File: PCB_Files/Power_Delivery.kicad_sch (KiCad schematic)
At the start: 0 parts

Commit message: Began laying out power schematic and motor controller schematic
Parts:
- added 5V_Buck_Module: Screw_Terminal_01x04, symbol Connector:Screw_Terminal_01x04
- added BT1: Battery, symbol Device:Battery
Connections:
- new net +5V: 5V_Buck_Module.2 (Pin_2)
- new net +BATT: 5V_Buck_Module.1 (Pin_1), BT1.1 (+)
- new net GND: 5V_Buck_Module.3 (Pin_3), 5V_Buck_Module.4 (Pin_4), BT1.2 (-)
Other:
- note added: "8V4 (Full) - 7V4 (Nom) - 6V4 (Cutoff)"

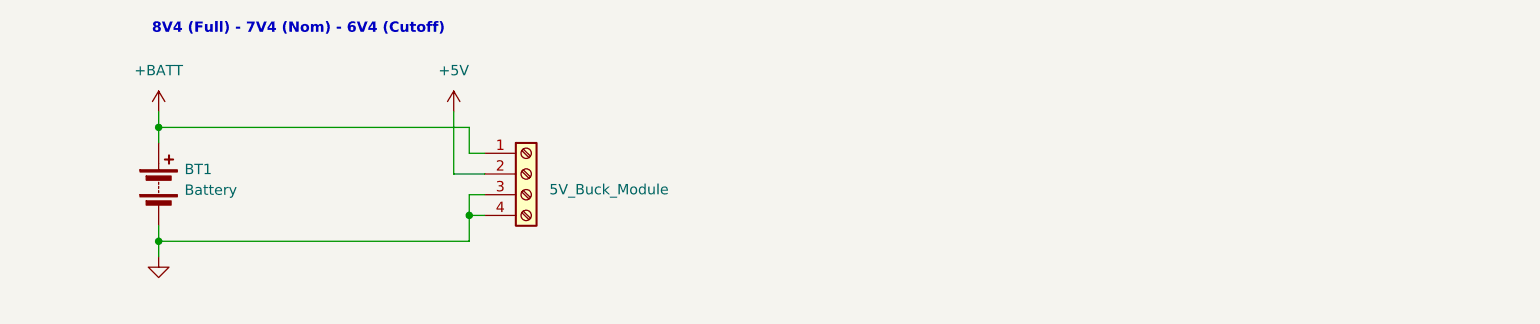
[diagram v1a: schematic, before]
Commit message: Completed power schematic page. 2S LiPo to buck module to LDO regulator for 3.3v
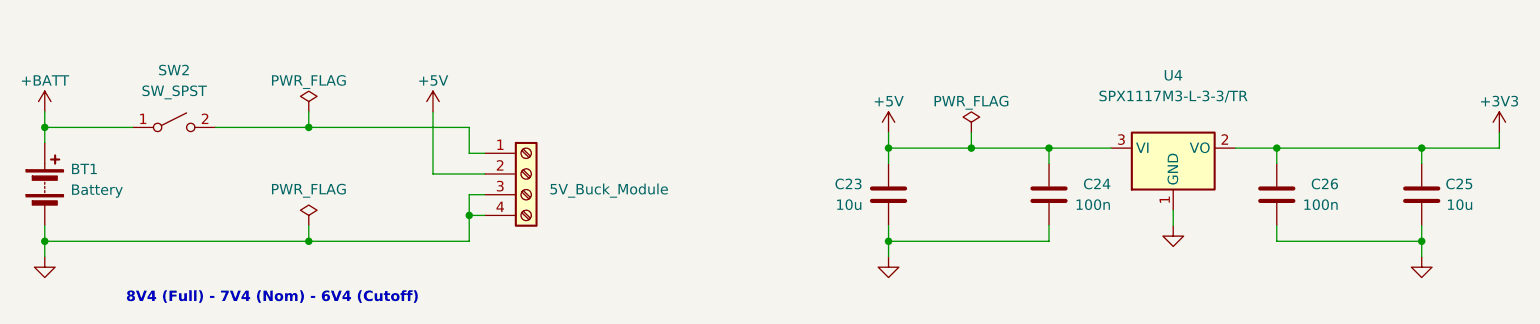
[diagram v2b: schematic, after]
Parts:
- added C23, C25: 10u, symbol Device:C
- added C24, C26: 100n, symbol Device:C
- added SW2: SW_SPST, symbol Switch:SW_SPST
- added U4: SPX1117M3-L-3-3/TR, Package_TO_SOT_SMD:SOT-223-3_TabPin2, symbol Regulator_Linear:AMS1117-3.3
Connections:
- net +5V: now also C23.1, C24.1, U4.3 (VI)
- net +BATT: now also SW2.1 (A); no longer 5V_Buck_Module.1 (Pin_1)
- net GND: now also C23.2, C24.2, C25.2, C26.2, U4.1 (GND)
- new net: 5V_Buck_Module.1 (Pin_1), SW2.2 (B)
- new net +3V3: C25.1, C26.1, U4.2 (VO)
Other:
- moved on the sheet: BT1

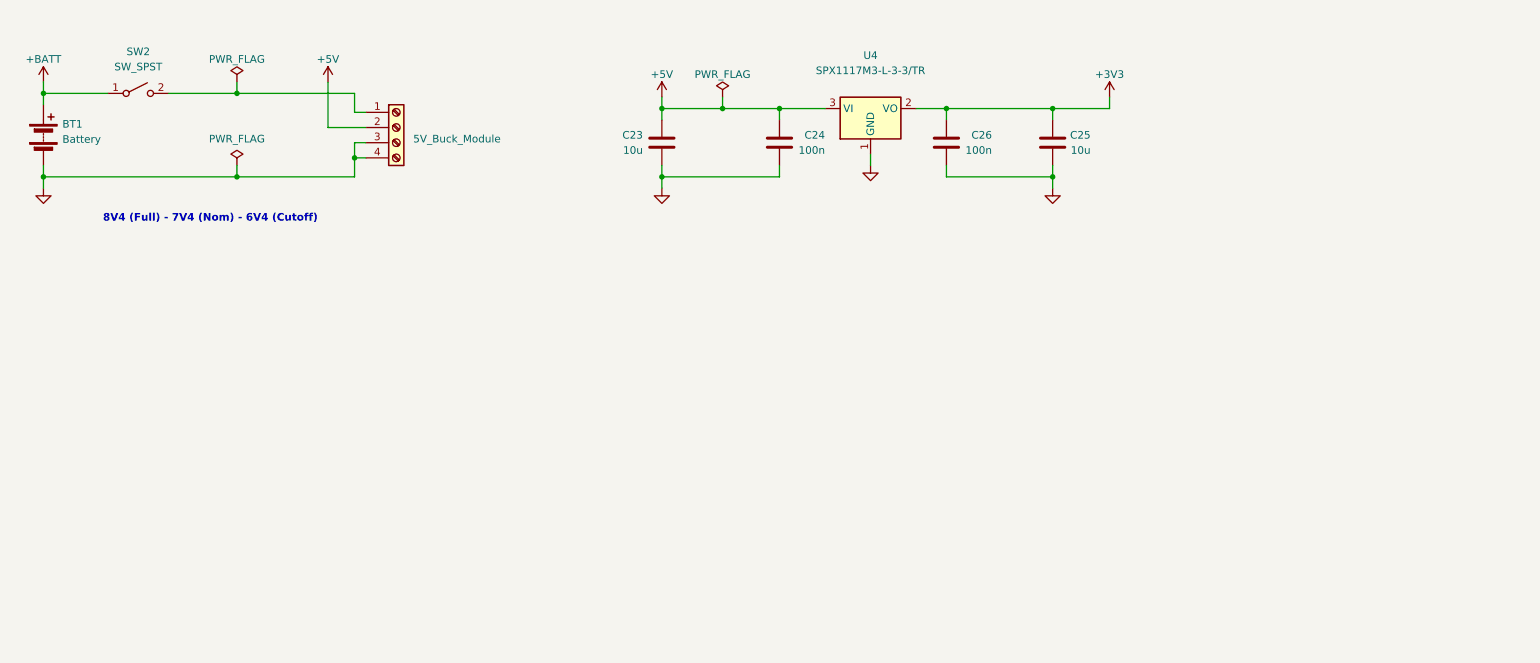
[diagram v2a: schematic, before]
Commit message: Cleaned up all ERC errors and warnings due to missing Power Flags or misaligned grid.
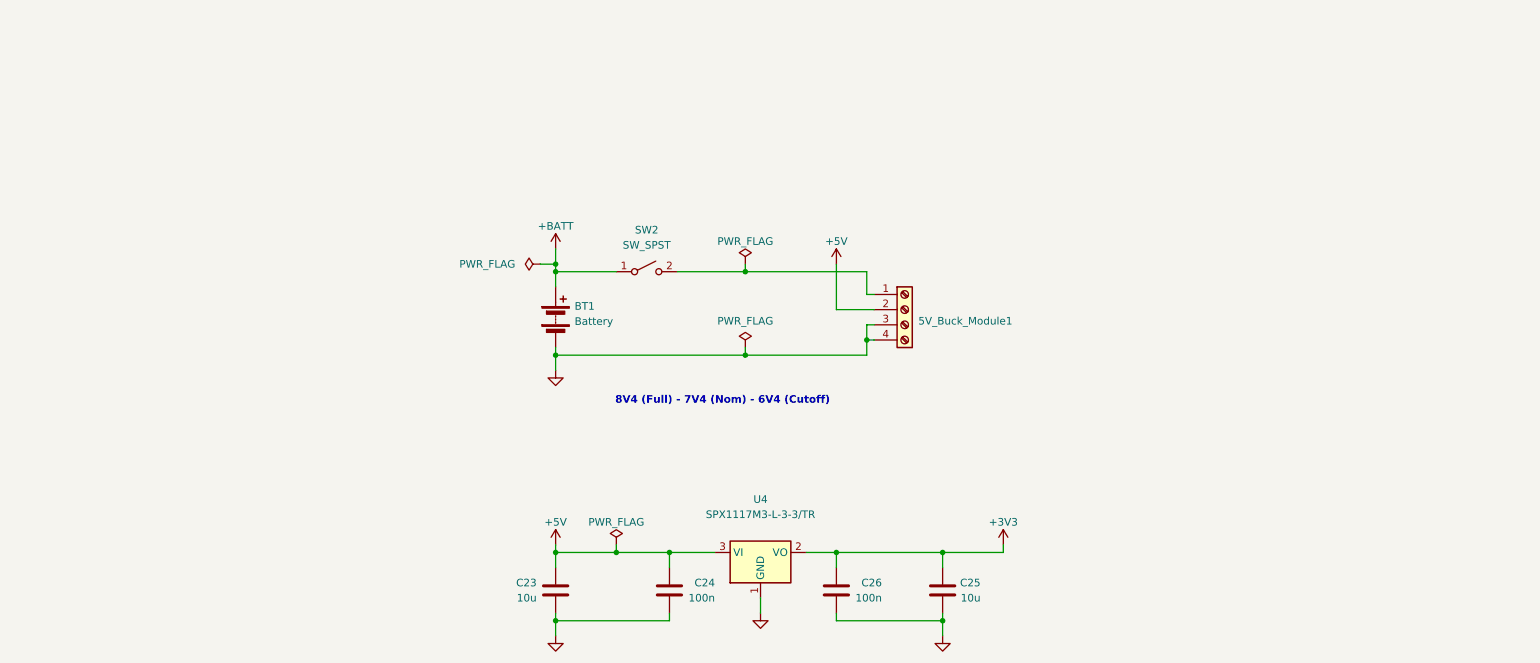
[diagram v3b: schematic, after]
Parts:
- renumbered 5V_Buck_Module to 5V_Buck_Module1
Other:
- moved on the sheet: 5V_Buck_Module1, BT1, C23, C24, C25, C26, SW2, U4

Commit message: General schematic clean up and footprint allocation.
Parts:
- C23, C24, C25, C26: footprint (none) -> Capacitor_SMD:C_0603_1608Metric
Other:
- moved on the sheet: 5V_Buck_Module1, BT1, C23, C24, C25, C26, SW2, U4

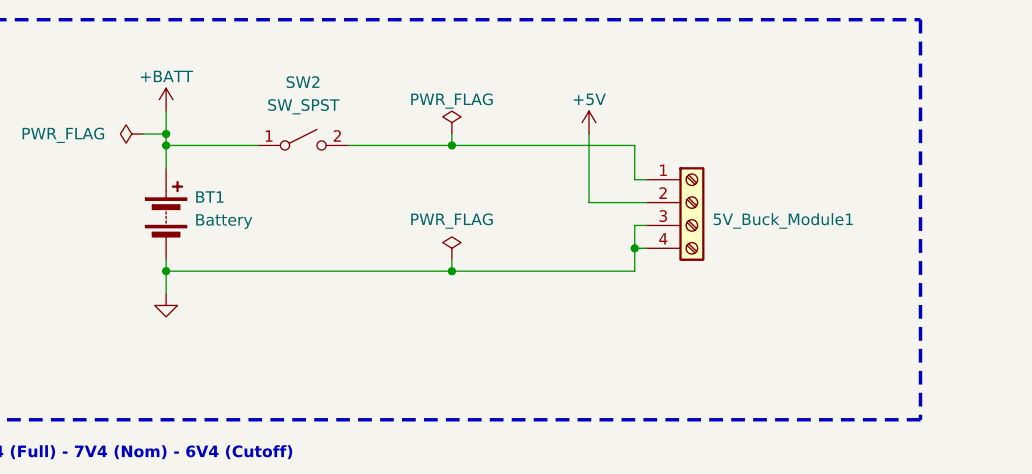
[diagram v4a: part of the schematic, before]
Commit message: Added RadioMaster 2S Battery information to power schematic sheet.
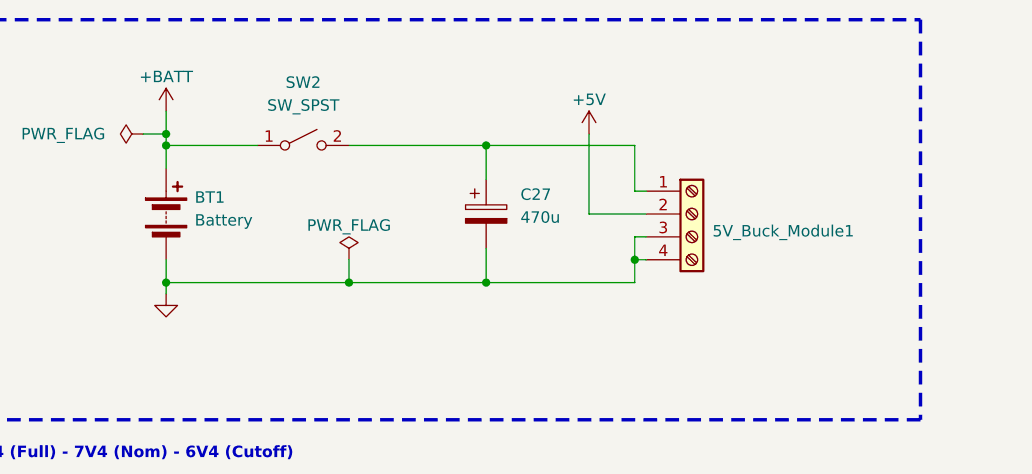
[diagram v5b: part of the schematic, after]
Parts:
- added C27: 470u, symbol Device:C_Polarized
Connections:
- net GND: now also C27.2
- net at 5V_Buck_Module1.1 (Pin_1), SW2.2 (B): now also C27.1
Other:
- moved on the sheet: 5V_Buck_Module1

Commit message: Cleaned up MCU sheet, added bounding boxes for peripherals.
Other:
- note added: "BATTERY INFO - Capacity: 5000mAh Watt Hours: 37wh Voltage: 7.4V Cells: 2 x 21700 Li-ion 3.7V 18.5Wh Connector: JST-XH and XT30 Charge current: Max 2A Dimensions: 71.5 x 43.5 x 23.5 mm Weight: 155g"
- note added: "RadioMaster 5000mAh 2s Li-ion"
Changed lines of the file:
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@@
 	(text "8V4 (Full) - 7V4 (Nom) - 6V4 (Cutoff)"
 		(exclude_from_sim no)
-		(at 38.1 80.01 0)
+		(at 38.1 85.09 0)
 		(effects
 			(font
@@
 		)
 	)
+	(text "RadioMaster 5000mAh 2s Li-ion"
+		(exclude_from_sim no)
+		(at 34.29 81.28 0)
+		(effects
+			(font
+				(size 1.27 1.27)
+				(thickness 0.254)
+				(bold yes)
+			)
+		)
+	)
+	(text "BATTERY INFO -\n\nCapacity: 5000mAh\n\nWatt Hours: 37wh\n\nVoltage: 7.4V\n\nCells: 2 x 21700 Li-ion 3.7V 18.5Wh\n\nConnector: JST-XH and XT30\n\nCharge current: Max 2A\n\nDimensions: 71.5 x 43.5 x 23.5 mm\n\nWeight: 155g"
+		(exclude_from_sim no)
+		(at 19.05 110.49 0)
+		(effects
+			(font
+				(size 1.27 1.27)
+				(thickness 0.254)
+				(bold yes)
+			)
+			(justify left)
+		)
+	)

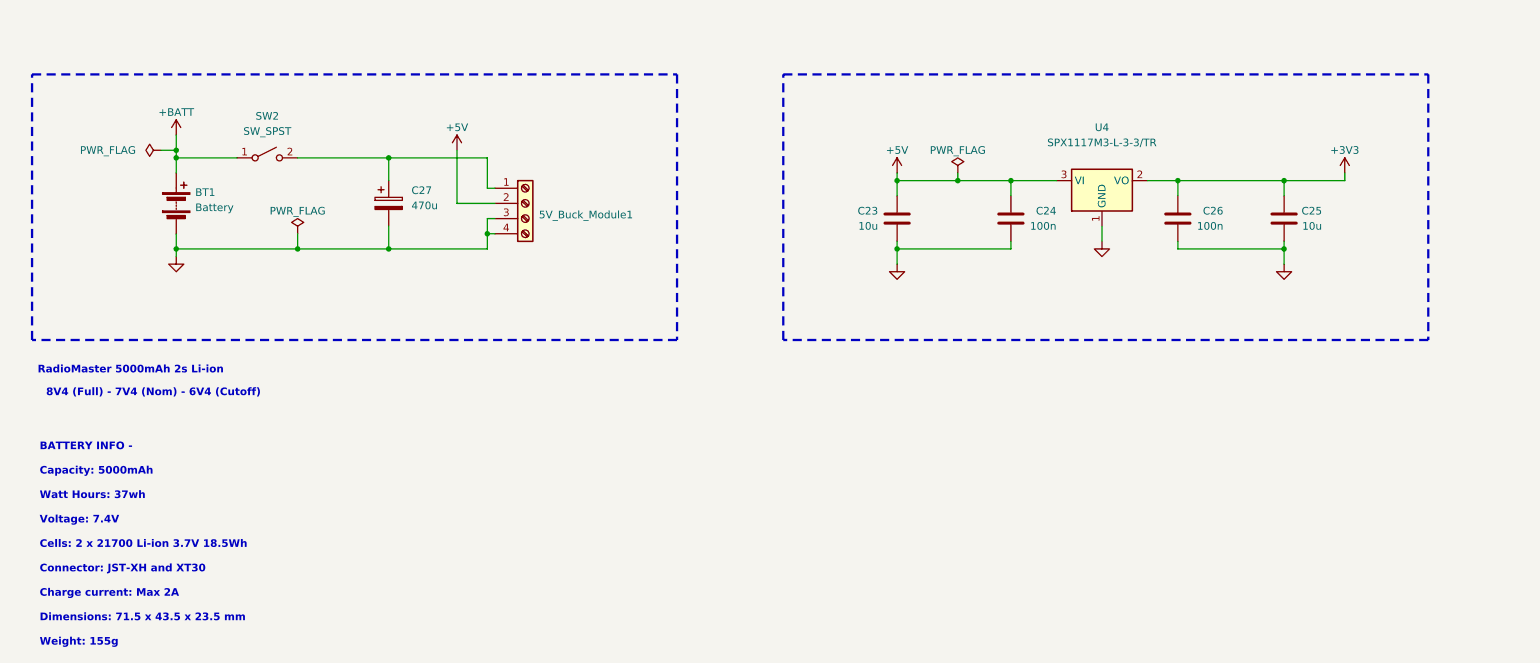
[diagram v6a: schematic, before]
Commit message: Added indicator and debug LED's to various outputs such as buck VOUT, ldo regulator VOUT, motor outputs, and status LED for MCU.
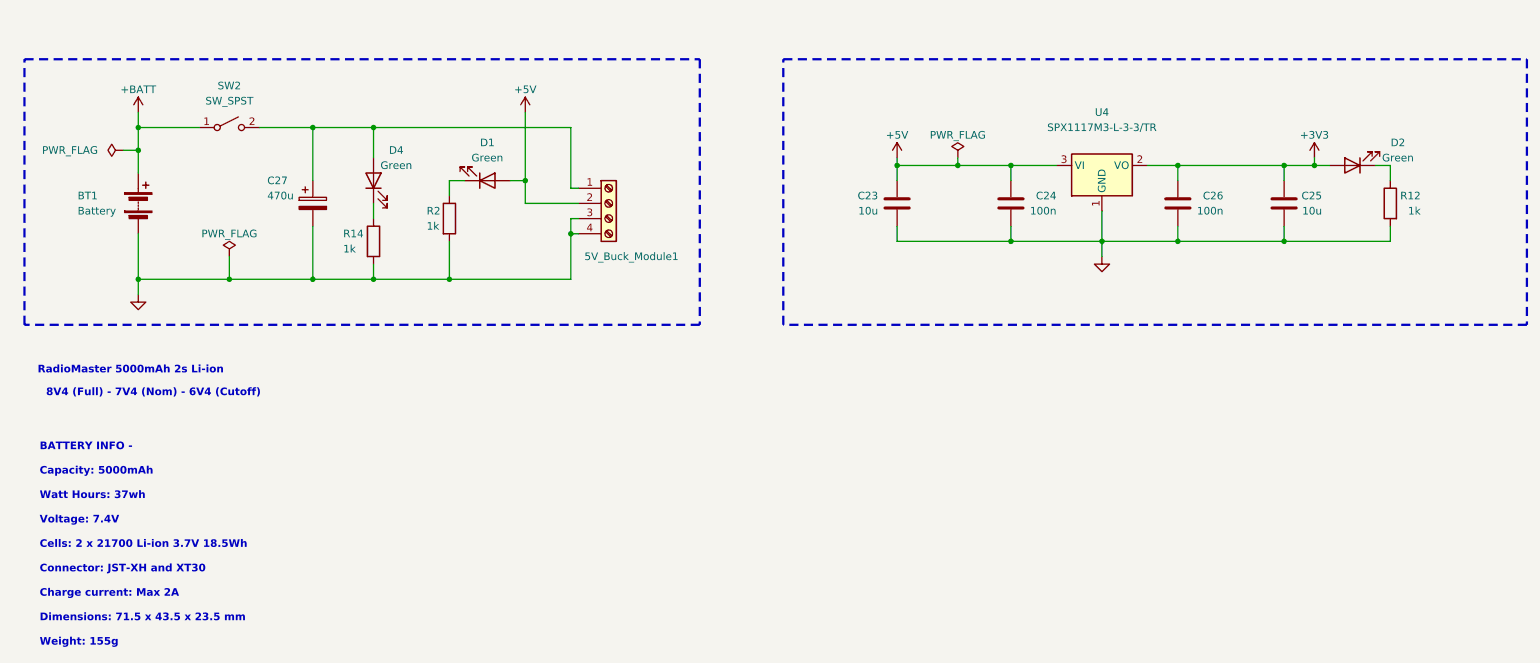
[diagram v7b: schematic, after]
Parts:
- added D1, D2, D4: Green, symbol Device:LED
- added R12, R14, R2: 1k, symbol Device:R
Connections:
- net +3V3: now also D2.2 (A)
- net +5V: now also D1.2 (A)
- net GND: now also R12.2, R14.2, R2.2
- net at 5V_Buck_Module1.1 (Pin_1), C27.1, SW2.2 (B): now also D4.2 (A)
- new net: D4.1 (K), R14.1
- new net: D1.1 (K), R2.1
- new net: D2.1 (K), R12.1
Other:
- moved on the sheet: 5V_Buck_Module1, BT1, C23, C24, C25, C26, C27, SW2, U4

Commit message: Added DNP to IMU pull up resistors due to already being on the module.
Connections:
- net +BATT_SW: now reaches 5V_Buck_Module1.1 (Pin_1), C27.1, D4.2 (A), SW2.2 (B)
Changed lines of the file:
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@@
+		)
+	)
+	(label "+BATT_SW"
+		(at 82.55 40.64 0)
+		(effects
+			(font
+				(size 1.27 1.27)
+				(thickness 0.254)
+				(bold yes)
+			)
+			(justify left bottom)
 		)
 	)
@@
 		(dnp no)
 		(property "Reference" "D4"
-			(at 78.74 44.45 90)
+			(at 71.12 49.53 90)
 			(show_name no)
 			(do_not_autoplace no)
@@
 		)
 		(property "Value" "Green"
-			(at 78.74 46.99 90)
+			(at 80.01 49.53 90)
 			(show_name no)
 			(do_not_autoplace no)
@@
 		(dnp no)
 		(property "Reference" "D1"
-			(at 93.98 43.18 0)
+			(at 93.98 46.99 0)
 			(show_name no)
 			(do_not_autoplace no)
@@
 		)
 		(property "Value" "Green"
-			(at 93.98 45.72 0)
+			(at 93.98 52.07 0)
 			(show_name no)
 			(do_not_autoplace no)
@@
 		(dnp no)
 		(property "Reference" "D2"
-			(at 246.38 43.18 0)
+			(at 238.76 44.45 0)
 			(show_name no)
 			(do_not_autoplace no)
@@
 		)
 		(property "Value" "Green"
-			(at 246.38 45.72 0)
-			(show_name no)
-			(do_not_autoplace no)
+			(at 238.76 49.53 0)
+			(show_name no)
+			(do_not_autoplace no)
